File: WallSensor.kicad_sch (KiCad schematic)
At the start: 5 parts, among them Q6 SiA519, U8 LBR-127HLD

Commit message: 新しい部品乗せた
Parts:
- C27: value 22 -> 22u; footprint Capacitor_SMD:C_0201_0603Metric -> Capacitor_SMD:C_0603_1608Metric
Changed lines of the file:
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@@
       (effects (font (size 1.27 1.27)) (justify left top))
     )
-    (property "Value" "22" (at 138.43 99.06 0)
+    (property "Value" "22u" (at 138.43 99.06 0)
       (effects (font (size 1.27 1.27)) (justify left bottom))
     )
-    (property "Footprint" "Capacitor_SMD:C_0201_0603Metric" (at 137.16 96.52 0)
+    (property "Footprint" "Capacitor_SMD:C_0603_1608Metric" (at 137.16 96.52 0)
       (effects (font (size 1.27 1.27)) hide)
     )
@@
       (effects (font (size 1.27 1.27) italic) hide)
     )
+    (pin "1")
+    (pin "2")
+    (pin "3")
+    (pin "4")
     (pin "5")
     (pin "6")
-    (pin "2")
-    (pin "1")
-    (pin "3")
-    (pin "4")
-    (instances
-      (project "micromouse_01_cp2"
+    (instances
+      (project "micromouse_01_cp2"

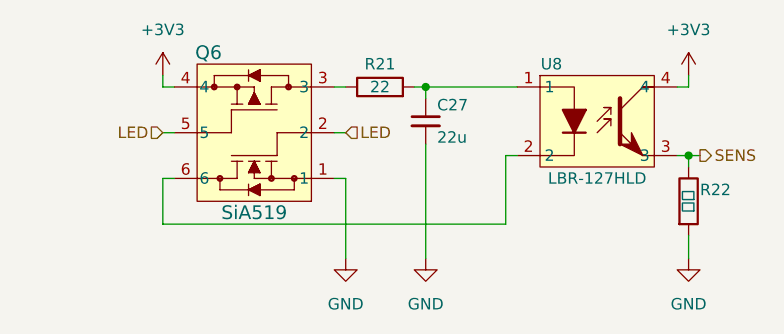
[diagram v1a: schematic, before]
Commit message: 回路図完成 PCB配線途中
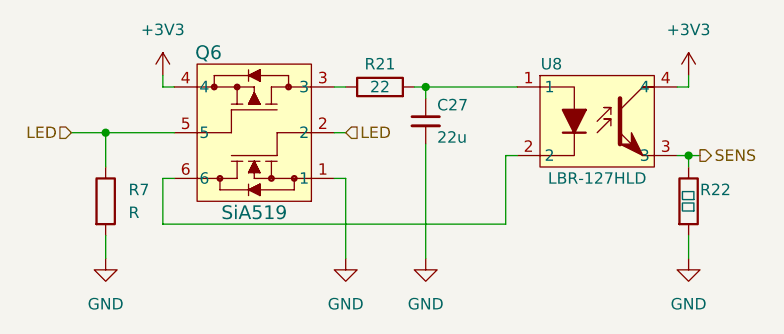
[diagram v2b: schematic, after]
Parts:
- added R7: R, symbol Device:R
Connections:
- net GND: now also R7.2
- net LED: now also R7.1
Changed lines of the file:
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@@
   (junction (at 137.16 92.71) (diameter 0) (color 0 0 0 0)
   )
+  (junction (at 101.6 97.79) (diameter 0) (color 0 0 0 0)
+  )
   (junction (at 166.37 100.33) (diameter 0) (color 0 0 0 0)
   )
@@
     (stroke (width 0) (type default))
   )
+  (wire (pts (xy 101.6 97.79) (xy 101.6 101.6))
+    (stroke (width 0) (type default))
+  )
   (wire (pts (xy 107.95 91.44) (xy 107.95 92.71))
     (stroke (width 0) (type default))
@@
     (stroke (width 0) (type default))
   )
+  (wire (pts (xy 101.6 97.79) (xy 109.22 97.79))
+    (stroke (width 0) (type default))
+  )
   (wire (pts (xy 166.37 91.44) (xy 166.37 92.71))
     (stroke (width 0) (type default))
@@
     (stroke (width 0) (type default))
   )
+  (wire (pts (xy 101.6 109.22) (xy 101.6 111.76))
+    (stroke (width 0) (type default))
+  )
   (wire (pts (xy 128.27 97.79) (xy 127 97.79))
     (stroke (width 0) (type default))
@@
     (stroke (width 0) (type default))
   )
-  (wire (pts (xy 107.95 97.79) (xy 109.22 97.79))
+  (wire (pts (xy 97.79 97.79) (xy 101.6 97.79))
     (stroke (width 0) (type default))
   )
@@
     (stroke (width 0) (type default))
   )
-  (hierarchical_label "LED" (shape input) (at 107.95 97.79 180) (fields_autoplaced)
+  (hierarchical_label "LED" (shape input) (at 97.79 97.79 180) (fields_autoplaced)
     (effects (font (size 1.27 1.27)) (justify right))
   )
@@
     )
   )
+  (symbol (lib_id "power:GND") (at 101.6 111.76 0) (unit 1)
+    (in_bom yes) (on_board yes) (dnp no) (fields_autoplaced)
+    (property "Reference" "#PWR03" (at 101.6 118.11 0)
+      (effects (font (size 1.27 1.27)) hide)
+    )
+    (property "Value" "GND" (at 101.6 116.84 0)
+      (effects (font (size 1.27 1.27)))
+    )
+    (property "Footprint" "" (at 101.6 111.76 0)
+      (effects (font (size 1.27 1.27)) hide)
+    )
+    (property "Datasheet" "" (at 101.6 111.76 0)
+      (effects (font (size 1.27 1.27)) hide)
+    )
+    (pin "1")
+    (instances
+      (project "micromouse_01_cp2"
+        (path "/619a00a9-cfa2-4255-85f4-bd5efe9f55d3/d924c110-d411-42e8-bf64-5ff34a3957e3/627fa30e-4c75-467d-8a11-fb456d2231a6"
+          (reference "#PWR03") (unit 1)
+        )
+        (path "/619a00a9-cfa2-4255-85f4-bd5efe9f55d3/d924c110-d411-42e8-bf64-5ff34a3957e3/a5cfc9e4-2fb5-4ee2-840f-6d7f10727bde"
+          (reference "#PWR038") (unit 1)
+        )
+        (path "/619a00a9-cfa2-4255-85f4-bd5efe9f55d3/d924c110-d411-42e8-bf64-5ff34a3957e3/b0d92089-ab2d-4e8e-8db9-4c15d2a8989d"
+          (reference "#PWR039") (unit 1)
+        )
+        (path "/619a00a9-cfa2-4255-85f4-bd5efe9f55d3/d924c110-d411-42e8-bf64-5ff34a3957e3/7e5f9c12-23d9-4717-a56b-443dd5a64a90"
+          (reference "#PWR043") (unit 1)
+        )
+      )
+    )
+  )
   (symbol (lib_id "New_Library:LBR-127HLD") (at 156.21 96.52 0) (unit 1)
     (in_bom yes) (on_board yes) (dnp no)
@@
         )
       )
+    )
+  )
+  (symbol (lib_id "Device:R") (at 101.6 105.41 0) (unit 1)
+    (in_bom yes) (on_board yes) (dnp no) (fields_autoplaced)
+    (property "Reference" "R7" (at 104.14 104.14 0)
+      (effects (font (size 1.27 1.27)) (justify left))
+    )
+    (property "Value" "R" (at 104.14 106.68 0)
+      (effects (font (size 1.27 1.27)) (justify left))
+    )
+    (property "Footprint" "" (at 99.822 105.41 90)
+      (effects (font (size 1.27 1.27)) hide)
+    )
+    (property "Datasheet" "~" (at 101.6 105.41 0)
+      (effects (font (size 1.27 1.27)) hide)
+    )
+    (pin "1")
+    (pin "2")
+    (instances
+      (project "micromouse_01_cp2"
+        (path "/619a00a9-cfa2-4255-85f4-bd5efe9f55d3/d924c110-d411-42e8-bf64-5ff34a3957e3/627fa30e-4c75-467d-8a11-fb456d2231a6"
+          (reference "R7") (unit 1)
+        )
+        (path "/619a00a9-cfa2-4255-85f4-bd5efe9f55d3/d924c110-d411-42e8-bf64-5ff34a3957e3/a5cfc9e4-2fb5-4ee2-840f-6d7f10727bde"
+          (reference "R10") (unit 1)
+        )
+        (path "/619a00a9-cfa2-4255-85f4-bd5efe9f55d3/d924c110-d411-42e8-bf64-5ff34a3957e3/b0d92089-ab2d-4e8e-8db9-4c15d2a8989d"
+          (reference "R13") (unit 1)
+        )
+        (path "/619a00a9-cfa2-4255-85f4-bd5efe9f55d3/d924c110-d411-42e8-bf64-5ff34a3957e3/7e5f9c12-23d9-4717-a56b-443dd5a64a90"
+          (reference "R29") (unit 1)
+        )
+      )

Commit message: Added 3D model
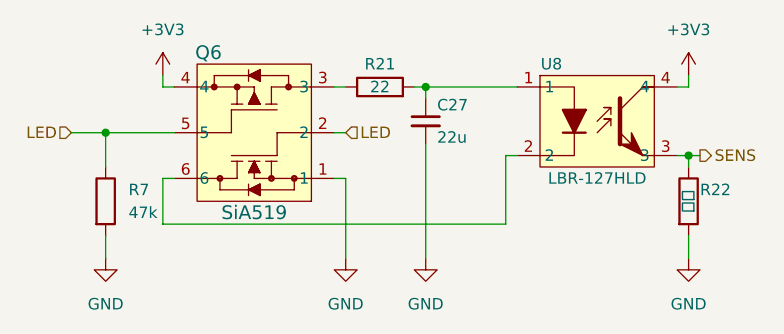
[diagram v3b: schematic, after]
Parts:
- R7: value R -> 47k; footprint (none) -> Resistor_SMD:R_0402_1005Metric
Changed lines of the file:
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@@
       (effects (font (size 1.27 1.27)) (justify left))
     )
-    (property "Value" "R" (at 104.14 106.68 0)
+    (property "Value" "47k" (at 104.14 106.68 0)
       (effects (font (size 1.27 1.27)) (justify left))
     )
-    (property "Footprint" "" (at 99.822 105.41 90)
+    (property "Footprint" "Resistor_SMD:R_0402_1005Metric" (at 99.822 105.41 90)
       (effects (font (size 1.27 1.27)) hide)
     )
